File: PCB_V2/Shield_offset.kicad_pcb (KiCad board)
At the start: 4 copper layers, 83.2 x 78.1 mm, 125 parts, among them J1 ADC, J10 I2C, J11 SERVO3, J12 SERVO4, J13 Power OUT, J2 BATT, J4 Screw_Terminal_01x04, J5 SERVO1, J6 ULTRA, J7 ENC1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

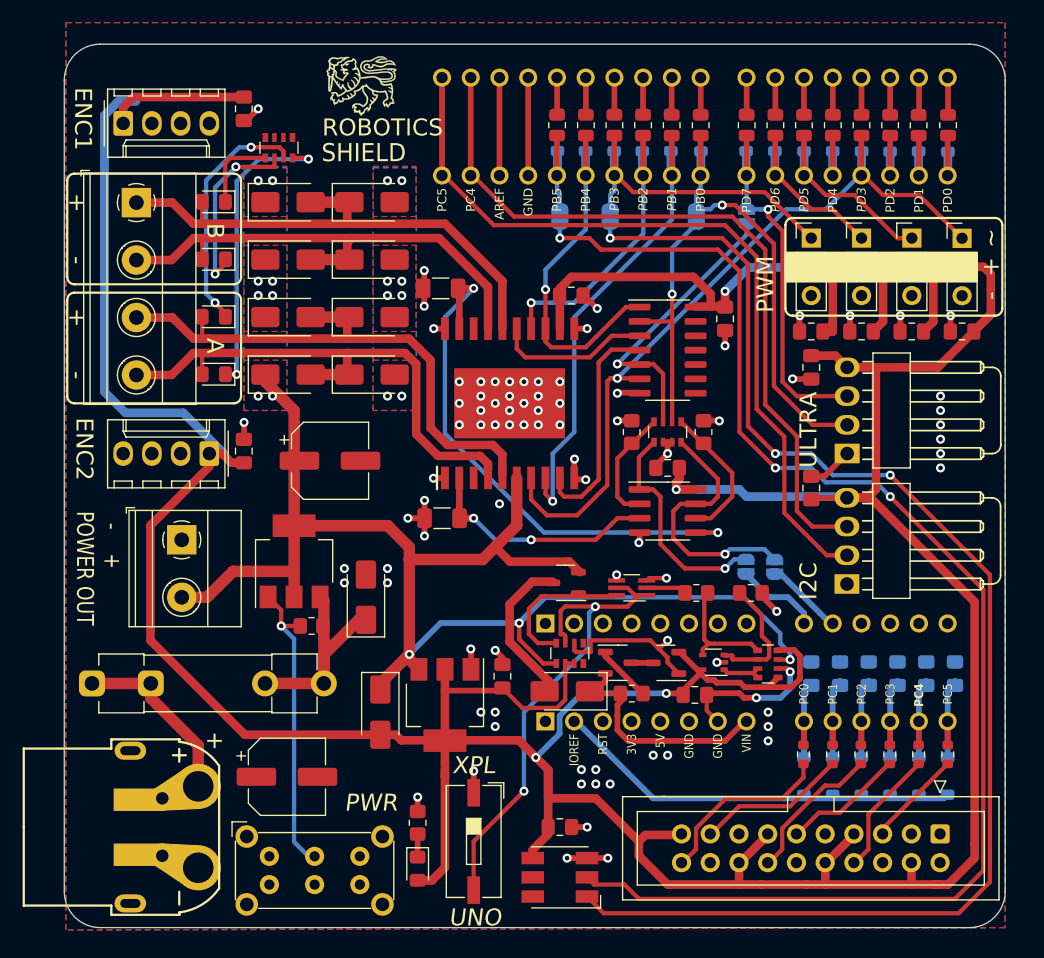
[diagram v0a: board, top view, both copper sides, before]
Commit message: Layout changes
Rearranged power supply components to better use space, removed components where possible from gap between offset headers.
Moved offset headers slightly to become aligned.
Added copper pours for high current nets
Removed F.Cu 5V tracks, inner layer plane is now used instead.
Swapped ENC1 and ENC2 to be consistent with motor phases.
Added silkscreen indicators for analogue, and updated power output header silk to match others.
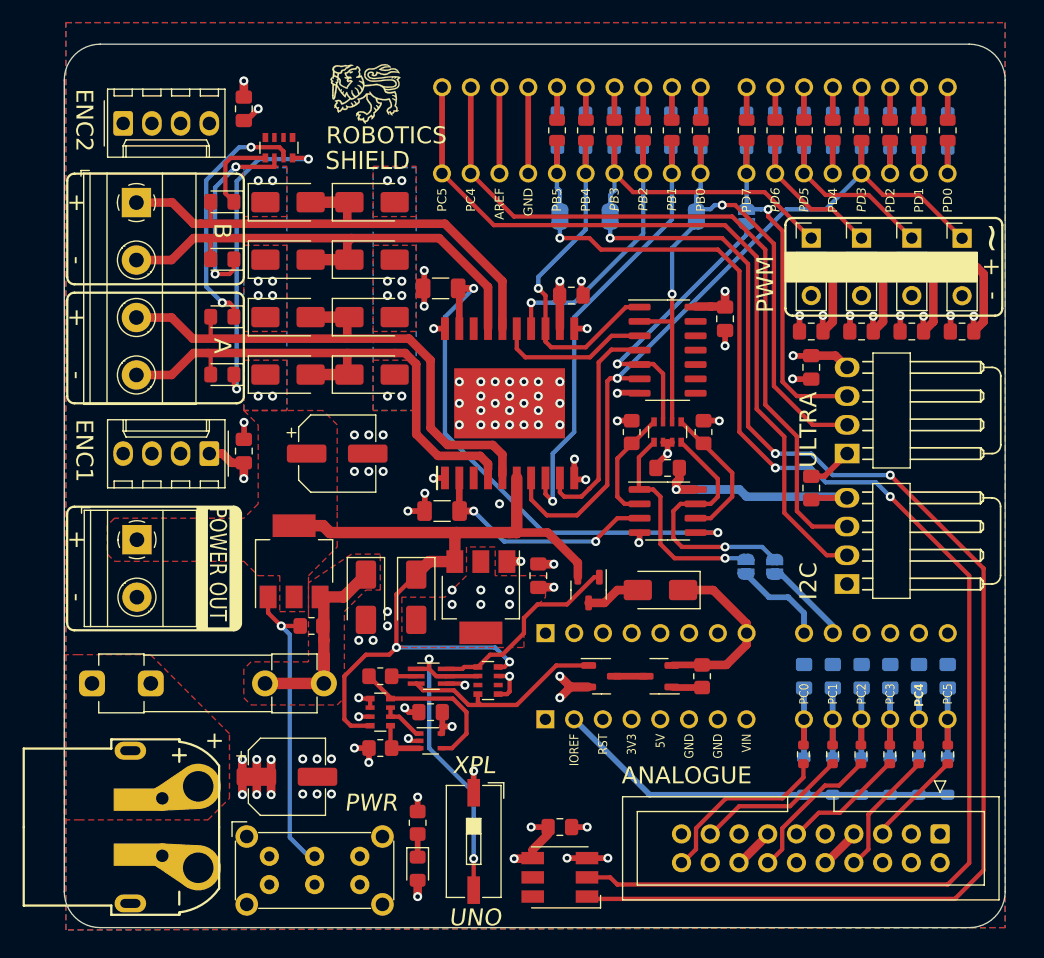
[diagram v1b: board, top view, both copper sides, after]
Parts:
- J9: value ENC2 -> ENC1
- moved R5 35.5 mm to (120.7, 84.5), turned to 180 degrees
- moved RN2 34.5 mm to (120.7, 81.3), turned to 0 degrees
- moved R6 28.9 mm to (120.7, 78.1), turned to 0 degrees
- moved U4 26.0 mm to (125.1, 83.8), turned to 0 degrees
- moved C6 23.4 mm to (125.1, 81.3), turned to 0 degrees
- moved Q2 19.4 mm to (125.2, 78.1), turned to 0 degrees
- moved D21 12.2 mm to (145.4, 70.5)
- moved D63 10.6 mm to (123.8, 71.1)
- moved U2 10.0 mm to (129.5, 71.1)
- moved C4 9.44 mm to (134.6, 69.2)
- moved RN4 7.62 mm to (130.2, 78.5), turned to 180 degrees
- moved R7 6.40 mm to (149.1, 78.1), turned to -90 degrees
- moved Q6 5.81 mm to (140.2, 78.1), turned to 0 degrees
- moved J13 3.96 mm to (99.1, 66.0)
- moved Q5 3.80 mm to (145.3, 78.1), turned to 180 degrees
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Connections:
- A1 pad 15: /ENC1B -> /ENC2B
- A1 pad 16: /ENC1A -> /ENC2A
- A1 pad 17: /ENC2A -> /ENC1A
- A1 pad 19: /ENC2B -> /ENC1B
- D23 pad 1: /ENC1B -> /ENC2B
- D26 pad 1: /ENC1A -> /ENC2A
- D28 pad 1: /ENC2A -> /ENC1A
- D38 pad 1: /ENC2B -> /ENC1B
- J13 pad 1: GND -> +BATT
- J13 pad 2: +BATT -> GND
- J7 pad 2: /ENC1A -> /ENC2A
- J7 pad 3: /ENC1B -> /ENC2B
- J9 pad 2: /ENC2A -> /ENC1A
- J9 pad 3: /ENC2B -> /ENC1B
- R16 pad 2: /ENC1B -> /ENC2B
- R17 pad 2: /ENC1A -> /ENC2A
- R18 pad 2: /ENC2A -> /ENC1A
- R23 pad 2: /ENC2B -> /ENC1B
- R5 pad 1: Net-(RN2C-R3.2) -> Net-(RN2D-R4.2)
- R6 pad 1: Net-(RN2D-R4.2) -> Net-(RN2A-R1.2)
- RN2 pad 2: GND -> +5V
- RN2 pad 3: +BATT -> GND
- RN2 pad 4: +5V -> +BATT
- RN2 pad 6: Net-(RN2C-R3.2) -> Net-(RN2B-R2.2)
- RN2 pad 7: Net-(RN2A-R1.2) -> Net-(RN2B-R2.2)
- RN4 pad 1: (no net) -> +5V
- RN4 pad 2: Net-(Q2B-D) -> (no net)
- RN4 pad 3: Net-(Q2A-S) -> +5V
- RN4 pad 4: Net-(Q2A-D) -> +BATT
- RN4 pad 5: +BATT -> Net-(Q2A-D)
- RN4 pad 6: +5V -> Net-(Q2A-S)
- RN4 pad 7: +5V -> (no net)
- RN4 pad 8: (no net) -> Net-(Q2B-D)
- U4 pad 1: Net-(RN2A-R1.2) -> Net-(RN2B-R2.2)
- U4 pad 3: Net-(RN2C-R3.2) -> Net-(RN2D-R4.2)
- U4 pad 4: Net-(RN2D-R4.2) -> Net-(RN2A-R1.2)
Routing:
- net +5V: track 423.6 -> 124.0 mm, vias 4 -> 31
- net +BATT: track 126.7 -> 70.6 mm, vias 11 -> 10
- net GND: track 97.6 -> 68.2 mm, vias 92 -> 85
- net Net-(J2-Pin_2): track 17.7 -> 0.00 mm
- net Net-(Q2A-S): track 42.5 -> 28.7 mm
- net Net-(RN2C-R3.2): track 11.1 -> 0.00 mm
- net Net-(RN2A-R1.2): track 3.82 -> 14.6 mm
- net /ENC2A: track 87.6 -> 78.0 mm
- net Net-(D21-A): track 13.8 -> 4.82 mm
- net /ENC2B: track 86.2 -> 77.6 mm
- net /ENC1A: track 78.6 -> 86.9 mm
- net /ENC1B: track 78.2 -> 85.8 mm
- net Net-(RN2D-R4.2): track 10.6 -> 3.84 mm
- net Vin: track 29.5 -> 23.6 mm
- net Net-(Q2A-D): track 13.2 -> 17.7 mm
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- added copper zone on F.Cu, net +5V
- added copper zone on F.Cu, net Net-(D4-K)
- added copper zone on F.Cu, net Net-(J2-Pin_2)
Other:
- board text added: "ANALOGUE"
- board text added: "POWER OUT"
- board text removed: "- + POWER OUT"
